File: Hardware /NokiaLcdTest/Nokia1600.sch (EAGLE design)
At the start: 9 parts

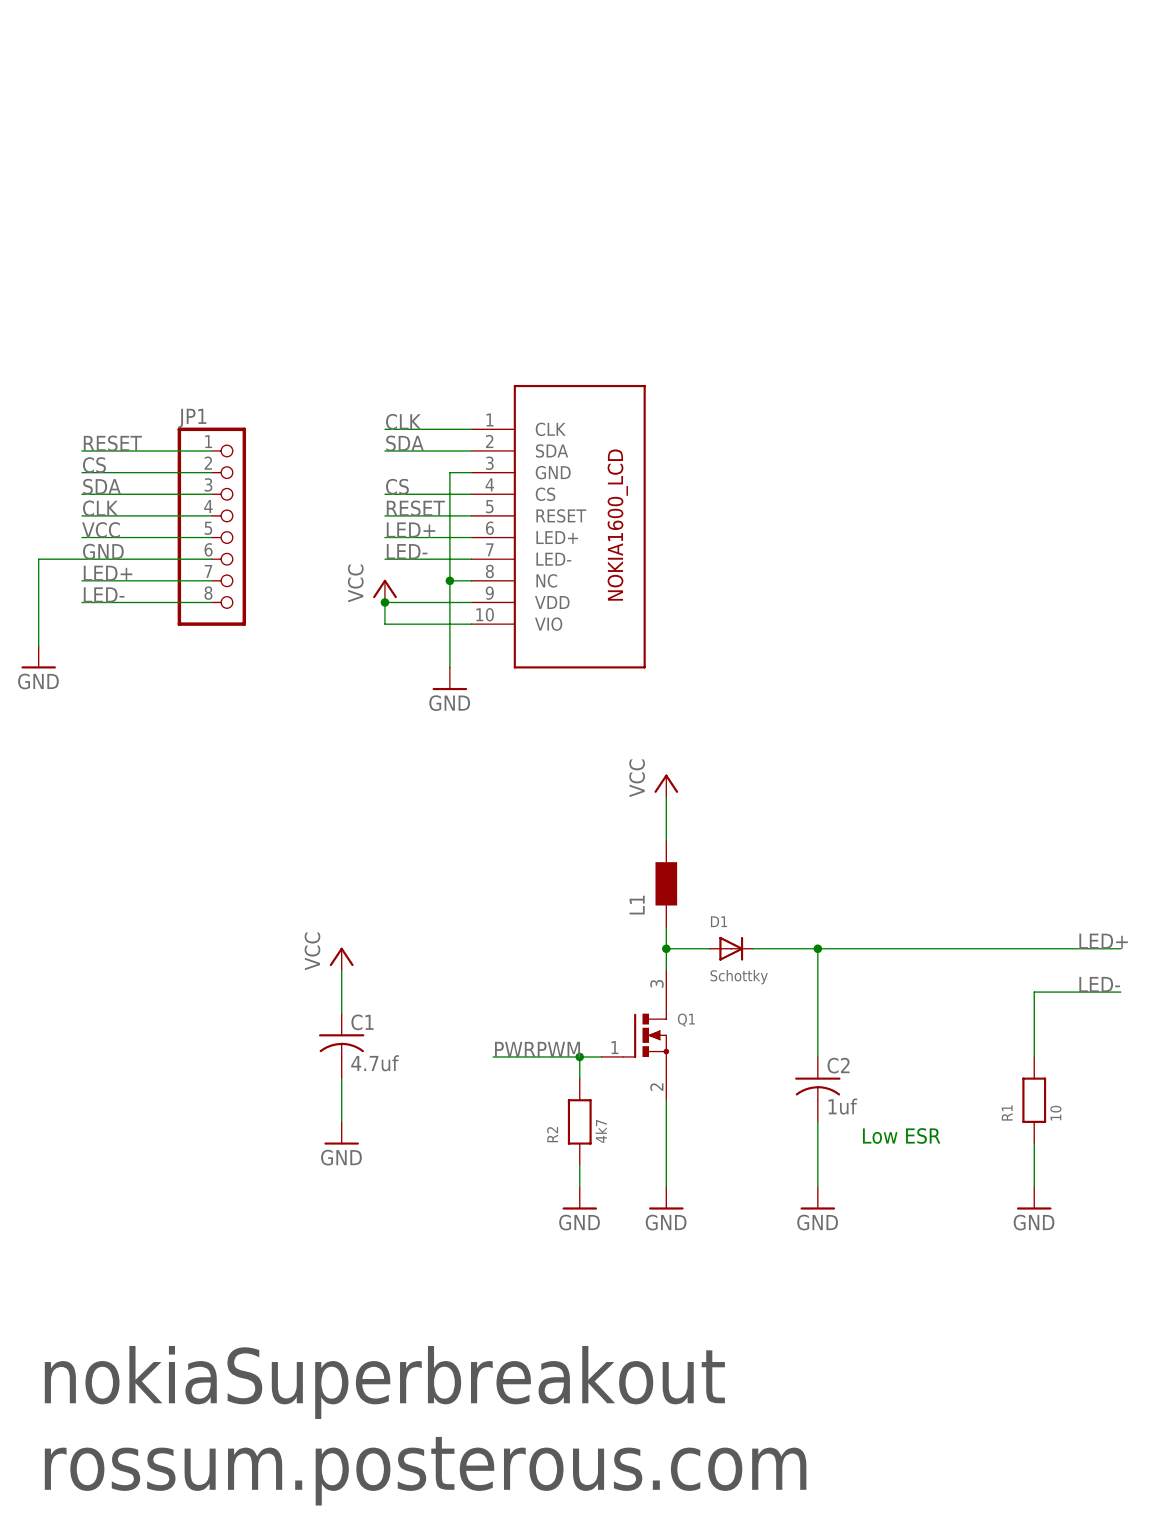
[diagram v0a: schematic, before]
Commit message: Trabajo en desarrollo CenditLab + hardware Cendit11713
   - Modulo Task, se crea clases para menejo de Instrumentos (Instrument)
   - Ediciones de esquematicos Cendit11714 + tarjeta Nokia 1600 LCD
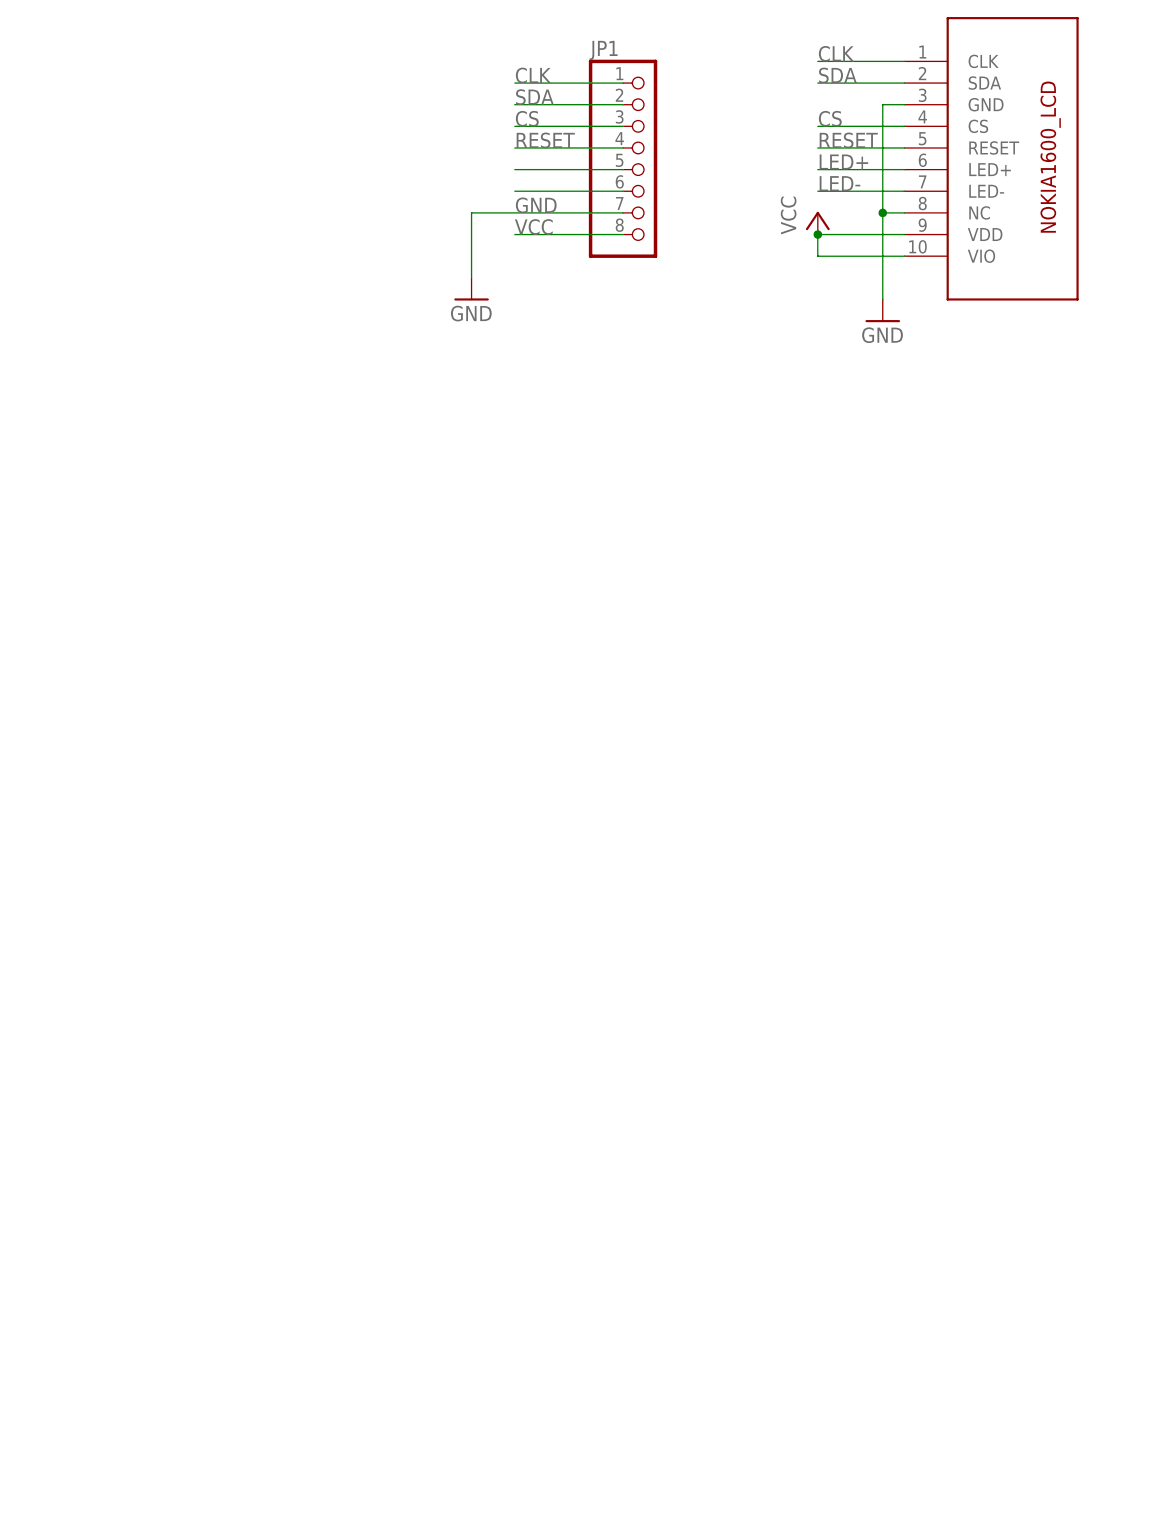
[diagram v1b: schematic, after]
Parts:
- removed C1: 4.7uf, adafruit:C-USC0805
- removed C2: 1uf, adafruit:C-USC0805
- removed D1: Schottky, microbuilder:DIODESOD-123
- removed L1: (no value), PeterAtMega644:WE-KIHQ_1008
- removed Q1: (no value), microbuilder:MOSFET-NREFLOW
- removed R1: 10, microbuilder:RESISTOR0805
- removed R2: 4k7, microbuilder:RESISTOR0805
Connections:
- removed net N$6: D1.A, L1.1, Q1.D
- removed net PWRPWM: Q1.G, R2.2
- net CLK: now also JP1.1; no longer JP1.4
- net CS: now also JP1.3; no longer JP1.2
- net GND: now also JP1.7; no longer C1.2, C2.2, JP1.6, Q1.S, R1.1, R2.1
- net LED+: now also JP1.5; no longer C2.1, D1.C, JP1.7
- net LED-: now also JP1.6; no longer JP1.8, R1.2
- net RESET: now also JP1.4; no longer JP1.1
- net SDA: now also JP1.2; no longer JP1.3
- net VCC: now also JP1.8; no longer C1.1, JP1.5, L1.2
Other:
- note removed: "Low ESR"
- note removed: "nokiaSuperbreakout"
- note removed: "rossum.posterous.com"
- moved on the sheet: JP1

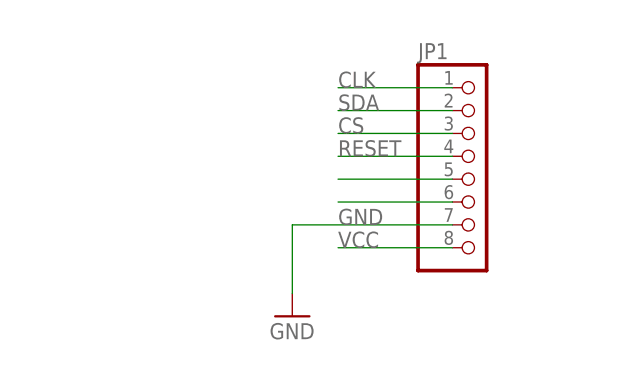
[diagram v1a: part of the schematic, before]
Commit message: Trabajo en Cenditlab + Tarjeta pantalla Nokia
  - En CenditLab trabajo en contenedor de datos para graficos GraphData
  - Instalador basico, v0.4
  - PCB para LCD nokia 1600 se agrega card header
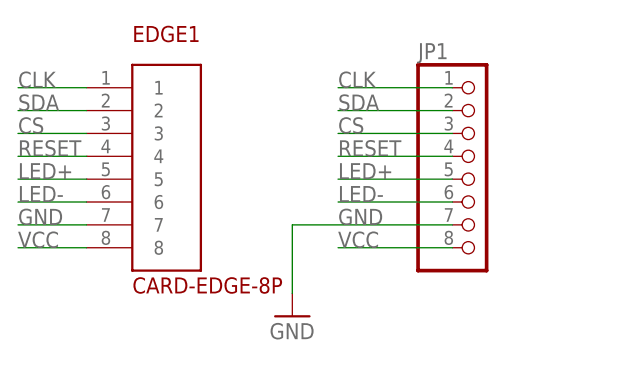
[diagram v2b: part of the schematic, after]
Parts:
- added EDGE1: CARD-EDGE-8P, SistemaCendit11713v2:DUOPLUG-8P-KEYEDCARD-EDGE-8P
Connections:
- net CLK: now also EDGE1.1
- net CS: now also EDGE1.3
- net GND: now also EDGE1.7
- net LED+: now also EDGE1.5
- net LED-: now also EDGE1.6
- net RESET: now also EDGE1.4
- net SDA: now also EDGE1.2
- net VCC: now also EDGE1.8
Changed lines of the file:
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@@
 <?xml version="1.0" encoding="utf-8"?>
 <!DOCTYPE eagle SYSTEM "eagle.dtd">
-<eagle version="7.7.0">
+<eagle version="7.2.0">
 <drawing>
 <settings>
@@
 <layer number="54" name="bGND_GNDA" color="1" fill="9" visible="no" active="no"/>
 <layer number="56" name="wert" color="7" fill="1" visible="no" active="no"/>
+<layer number="90" name="Modules" color="5" fill="1" visible="yes" active="yes"/>
 <layer number="91" name="Nets" color="2" fill="1" visible="yes" active="yes"/>
 <layer number="92" name="Busses" color="1" fill="1" visible="yes" active="yes"/>
@@
 <part name="GND1" library="supply1" deviceset="GND" device=""/>
 <part name="FRAME1" library="frames" deviceset="LETTER_L" device=""/>
+<part name="EDGE1" library="SistemaCendit11713v2" deviceset="DUOPLUG-8P-KEYED" device="CARD-EDGE-8P" value="CARD-EDGE-8P"/>
 </parts>
 <sheets>
@@
 <instance part="FRAME1" gate="G$1" x="-332.74" y="-30.48"/>
 <instance part="FRAME1" gate="G$2" x="-185.42" y="-30.48"/>
+<instance part="EDGE1" gate="G$1" x="-264.16" y="76.2"/>
 </instances>
 <busses>
@@
 <label x="-243.84" y="68.58" size="1.778" layer="95"/>
 </segment>
+<segment>
+<label x="-279.4" y="68.58" size="1.778" layer="95"/>
+<pinref part="EDGE1" gate="G$1" pin="7"/>
+<wire x1="-271.78" y1="68.58" x2="-279.4" y2="68.58" width="0.1524" layer="91"/>
+</segment>
 </net>
 <net name="VCC" class="1">
@@
 <label x="-243.84" y="66.04" size="1.778" layer="95"/>
 </segment>
+<segment>
+<label x="-279.4" y="66.04" size="1.778" layer="95"/>
+<pinref part="EDGE1" gate="G$1" pin="8"/>
+<wire x1="-271.78" y1="66.04" x2="-279.4" y2="66.04" width="0.1524" layer="91"/>
+</segment>
 </net>
 <net name="LED+" class="1">
@@
 <pinref part="JP1" gate="A" pin="5"/>
 <wire x1="-231.14" y1="73.66" x2="-243.84" y2="73.66" width="0.1524" layer="91"/>
+<label x="-243.84" y="73.66" size="1.778" layer="95"/>
+</segment>
+<segment>
+<pinref part="EDGE1" gate="G$1" pin="5"/>
+<wire x1="-271.78" y1="73.66" x2="-279.4" y2="73.66" width="0.1524" layer="91"/>
+<label x="-279.4" y="73.66" size="1.778" layer="95"/>
 </segment>
 </net>
@@
 <label x="-243.84" y="76.2" size="1.778" layer="95"/>
 </segment>
+<segment>
+<pinref part="EDGE1" gate="G$1" pin="4"/>
+<wire x1="-271.78" y1="76.2" x2="-279.4" y2="76.2" width="0.1524" layer="91"/>
+<label x="-279.4" y="76.2" size="1.778" layer="95"/>
+</segment>
 </net>
 <net name="SDA" class="0">
@@
 <label x="-243.84" y="81.28" size="1.778" layer="95"/>
 </segment>
+<segment>
+<pinref part="EDGE1" gate="G$1" pin="2"/>
+<wire x1="-271.78" y1="81.28" x2="-279.4" y2="81.28" width="0.1524" layer="91"/>
+<label x="-279.4" y="81.28" size="1.778" layer="95"/>
+</segment>
 </net>
 <net name="CLK" class="0">
@@
 <label x="-243.84" y="83.82" size="1.778" layer="95"/>
 </segment>
+<segment>
+<wire x1="-271.78" y1="83.82" x2="-279.4" y2="83.82" width="0.1524" layer="91"/>
+<label x="-279.4" y="83.82" size="1.778" layer="95"/>
+<pinref part="EDGE1" gate="G$1" pin="1"/>
+</segment>
 </net>
 <net name="CS" class="0">
@@
 <label x="-243.84" y="78.74" size="1.778" layer="95"/>
 </segment>
+<segment>
+<pinref part="EDGE1" gate="G$1" pin="3"/>
+<wire x1="-271.78" y1="78.74" x2="-279.4" y2="78.74" width="0.1524" layer="91"/>
+<label x="-279.4" y="78.74" size="1.778" layer="95"/>
+</segment>
 </net>
 <net name="LED-" class="0">
@@
 <pinref part="JP1" gate="A" pin="6"/>
 <wire x1="-231.14" y1="71.12" x2="-243.84" y2="71.12" width="0.1524" layer="91"/>
-</segment>
-</net>
+<label x="-243.84" y="71.12" size="1.778" layer="95"/>
+</segment>
+<segment>
+<pinref part="EDGE1" gate="G$1" pin="6"/>
+<wire x1="-271.78" y1="71.12" x2="-279.4" y2="71.12" width="0.1524" layer="91"/>
+<label x="-279.4" y="71.12" size="1.778" layer="95"/>
+</segment>
+</net>
